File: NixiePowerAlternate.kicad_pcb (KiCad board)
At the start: 2 copper layers, 100 x 50 mm, 27 parts, among them J1 12VDC, J2 Screw_Terminal_01x02, J3 Screw_Terminal_01x03, J4 Screw_Terminal_01x03, U1 AMS1117-5.0, U2 MAX1771ESA, U3 AMS1117-3.3

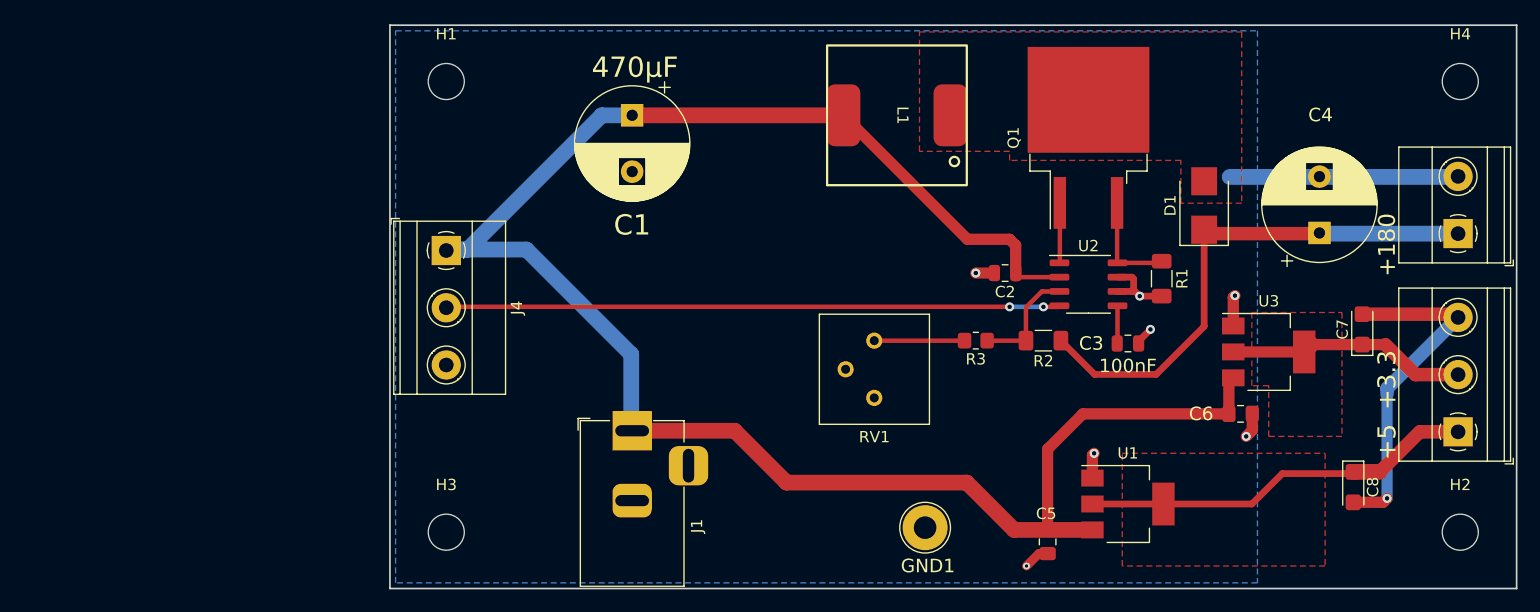
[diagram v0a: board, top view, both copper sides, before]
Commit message: Add files via upload
Checked L1 and Q1 against recommendations in the datasheet.  Decided to keep as is.  The MOSFET is fine.  L1 should be too and it is rated for 400V. 
Added feed forward capacitor C9, 47pF in parallel with R2.    The datasheet suggests values between 47pF and 220pF, using the lowest that insures stability.  The design is stable in PSPICE without the cap.  In practice it may be optional. 

Updated the PCB with the parts changes and fixed a layout error from Rev 0.
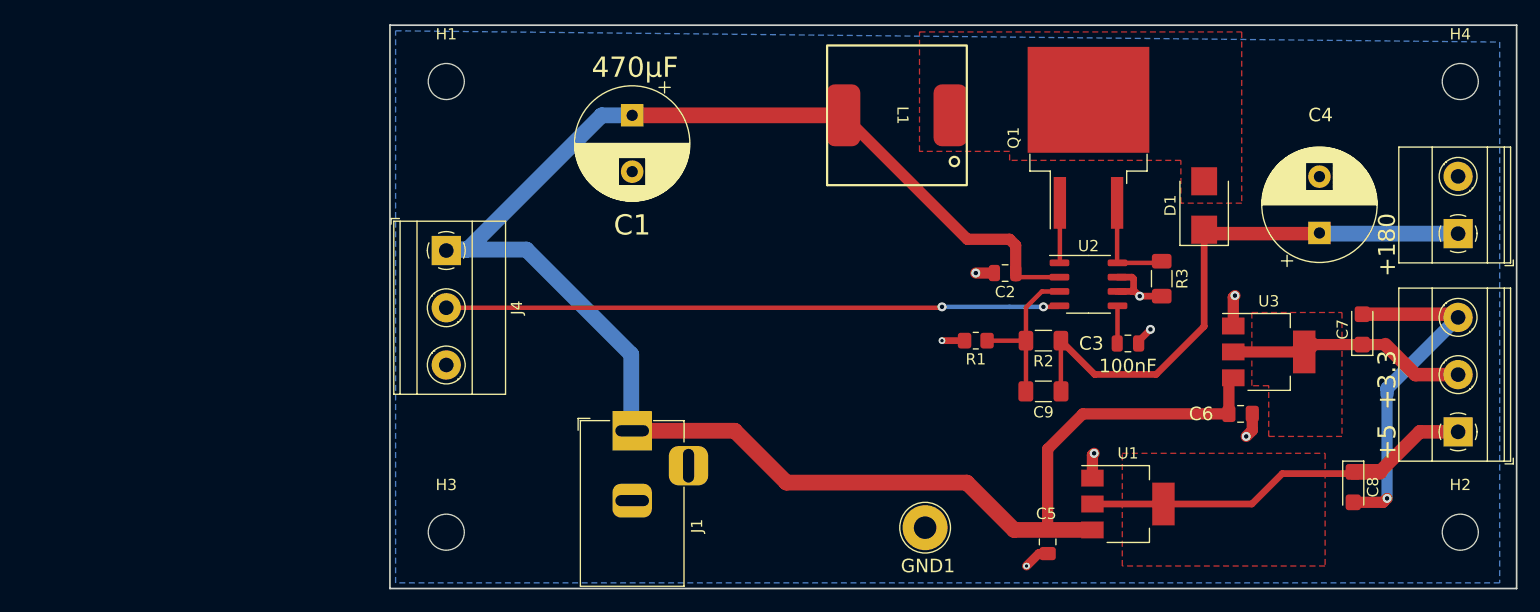
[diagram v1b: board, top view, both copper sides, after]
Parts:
- removed RV1: 5K, Potentiometer_THT:Potentiometer_Bourns_3386P_Vertical
- added C9: 47pF, Capacitor_SMD:C_1206_3216Metric_Pad1.33x1.80mm_HandSolder, F.Cu at (158.0, 132.5)
- C4: value 3.3µF 400V -> 3.3µF
- R1: renamed from R3; value 6.8K -> 10K
- R2: value 1.2M -> 1.18M
- renumbered R1 to R3
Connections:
- R1 pad 2: Net-(R3-Pad2) -> GND
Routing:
- net GND: track 70.5 -> 52.1 mm, vias 8 -> 9
- net Net-(R3-Pad2): track 8.01 -> 0.00 mm
- net Net-(R1-Pad1): track 9.96 -> 14.5 mm
- net Net-(C4-Pad1): track 47.2 -> 51.7 mm

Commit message: Add files via upload
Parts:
- removed the C5 at (158.4, 145.9)
- removed the U1 at (165.5, 142.5)
- added C10: 100uF, Capacitor_Tantalum_SMD:CP_EIA-3528-21_Kemet-B_Pad1.50x2.35mm_HandSolder, F.Cu at (90.5, 107.6)
- added C11: 100uF, Capacitor_Tantalum_SMD:CP_EIA-3528-21_Kemet-B_Pad1.50x2.35mm_HandSolder, F.Cu at (79.9, 119.9)
- added C12: 4.7uF, Capacitor_SMD:C_1206_3216Metric_Pad1.33x1.80mm_HandSolder, F.Cu at (135.0, 140.0)
- added C13: 4.7uF, Capacitor_SMD:C_1206_3216Metric_Pad1.33x1.80mm_HandSolder, F.Cu at (139.0, 140.0)
- added C14: 4.7uF, Capacitor_SMD:C_1206_3216Metric_Pad1.33x1.80mm_HandSolder, F.Cu at (143.0, 140.0)
- added C8: 10nF, Capacitor_SMD:C_0805_2012Metric_Pad1.18x1.45mm_HandSolder, F.Cu at (158.0, 140.0)
- added D2: SS34, Diode_SMD:D_SMA_Handsoldering, F.Cu at (156.0, 145.0)
- added L2: 47uH, CoilCraft:L_CoilCraft_MSS1048, F.Cu at (72.7, 111.6)
- added R4: 10K, Resistor_SMD:R_0805_2012Metric_Pad1.20x1.40mm_HandSolder, F.Cu at (164.0, 140.0)
- added R5: 3.24K, Resistor_SMD:R_0805_2012Metric_Pad1.20x1.40mm_HandSolder, F.Cu at (164.0, 136.0)
- added U3: TPS5430DDA, Package_SO:TI_SO-PowerPAD-8_ThermalVias, F.Cu at (151.0, 138.0)
- C7: value 10uF -> 100uF; footprint Capacitor_Tantalum_SMD:CP_EIA-3216-18_Kemet-A -> Capacitor_Tantalum_SMD:CP_EIA-3528-21_Kemet-B_Pad1.50x2.35mm_HandSolder
- C9: renamed from C8; value 10uF -> 100uF; footprint Capacitor_Tantalum_SMD:CP_EIA-3216-18_Kemet-A -> Capacitor_Tantalum_SMD:CP_EIA-3528-21_Kemet-B_Pad1.50x2.35mm_HandSolder
- moved GND1 30.7 mm to (134.0, 117.0)
- moved C7 1.04 mm to (186.0, 126.0)
- renumbered C4 to C3, C9 to C4, C3 to C5, J2 to J1, J4 to J2, J1 to J3, J3 to J4, R2 to R1, R3 to R2, R1 to R3, U2 to U1, U3 to U2
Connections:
- net +3.3V renamed Net-(C7-Pad1)
- C6 pad 1: +12V -> +5V
- U2 pad 3: +12V -> +5V
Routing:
- net +12V: track 167.2 -> 103.9 mm
- net GND: track 52.1 -> 39.2 mm, vias 9 -> 7
- net +5V: track 35.1 -> 24.3 mm
- removed copper zone on F.Cu, net +5V

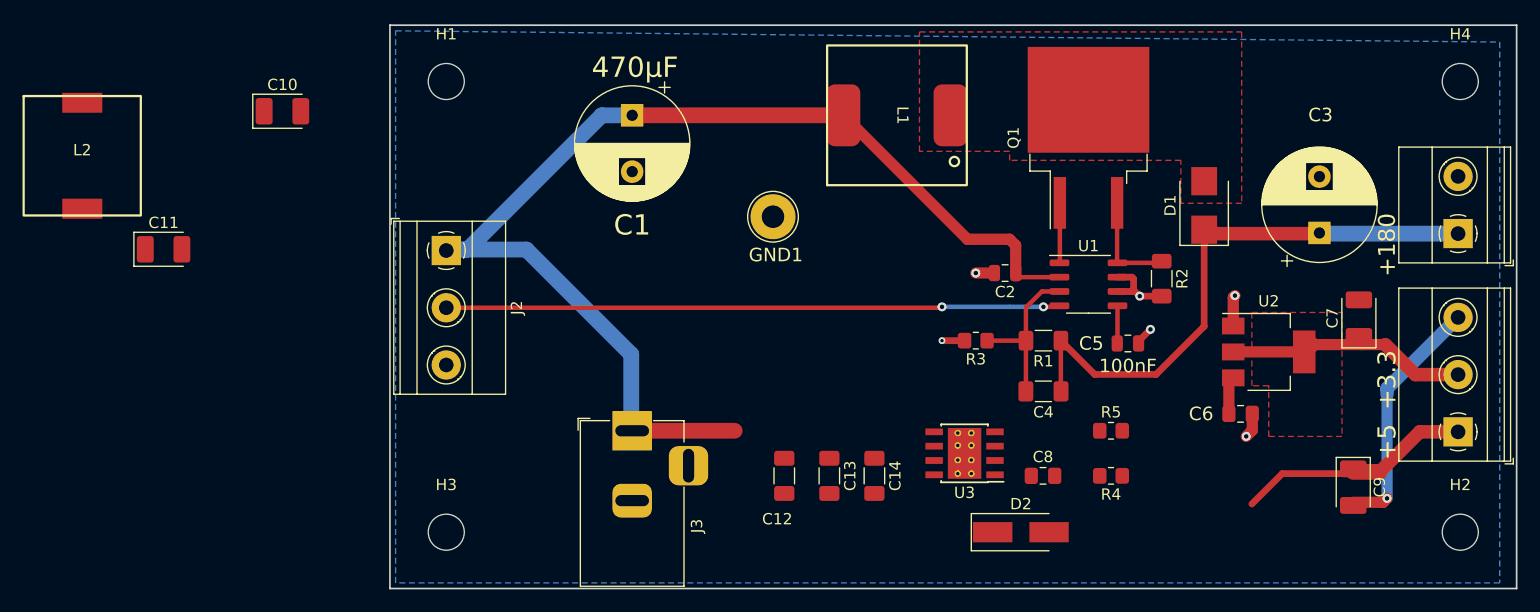
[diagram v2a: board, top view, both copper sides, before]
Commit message: Add files via upload
Need to reduce cost before submitting for production.
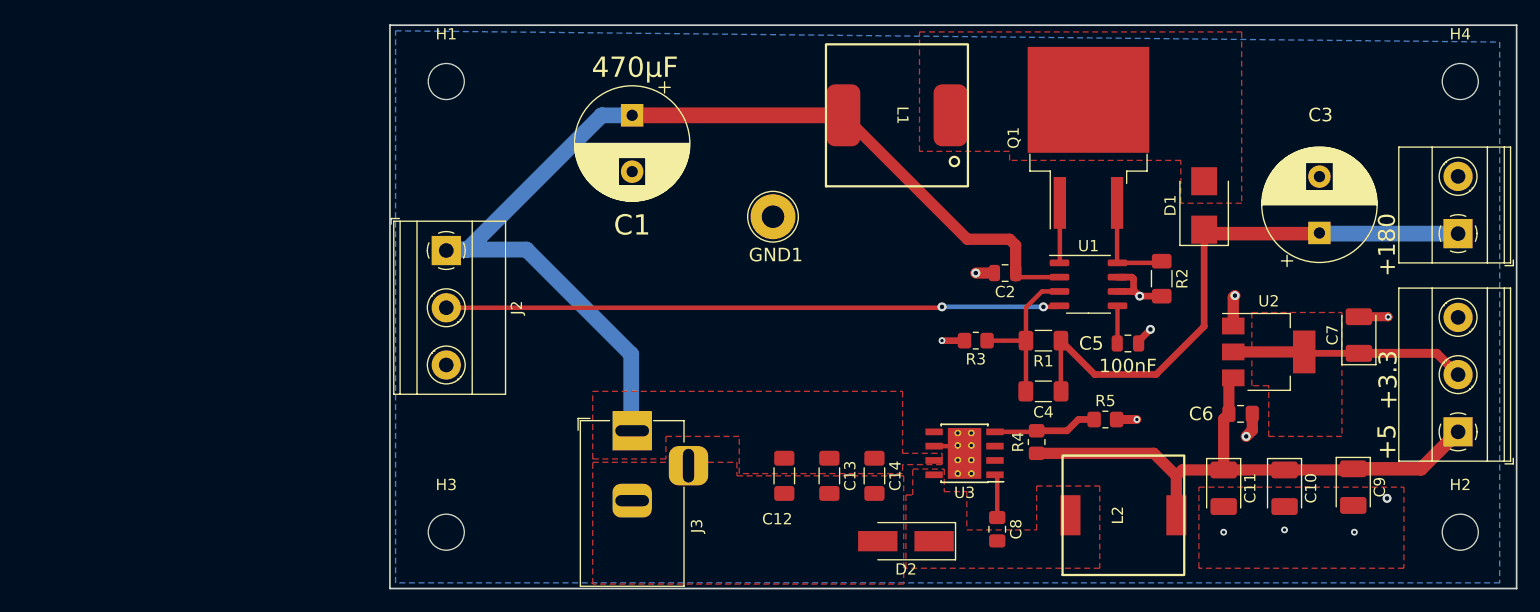
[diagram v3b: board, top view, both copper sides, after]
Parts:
- moved L2 97.8 mm to (165.1, 143.5), turned to 90 degrees
- moved C11 96.5 mm to (174.0, 141.1), turned to -90 degrees
- moved C10 95.0 mm to (179.4, 141.1), turned to -90 degrees
- moved D2 10.2 mm to (145.8, 145.8), turned to 180 degrees
- moved R4 7.25 mm to (157.4, 137.0), turned to 90 degrees
- moved C8 6.24 mm to (153.9, 144.7), turned to -90 degrees
- moved C7 1.50 mm to (186.0, 127.5)
- moved R5 1.12 mm to (163.5, 135.0)
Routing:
- net +5V: track 24.3 -> 51.9 mm
- net GND: track 39.2 -> 24.4 mm, vias 7 -> 12
- net Net-(R4-Pad2): track 0.00 -> 9.25 mm
- net +12V: track 103.9 -> 94.8 mm
- net Net-(C8-Pad1): track 0.00 -> 3.88 mm
- net Net-(C7-Pad1): track 21.3 -> 20.8 mm
- added copper zone on F.Cu, net +12V
- added copper zone on F.Cu, net GND
- added copper zone on F.Cu, net Net-(C8-Pad2)

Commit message: Add files via upload
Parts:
- C12, C13, C14: value 4.7uF -> 10uF
- C6: value 1uF -> 100nF
- D1: value ~ -> ES2F
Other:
- board text added: "Rev 0.3 09022023 Andrew Fischer"
